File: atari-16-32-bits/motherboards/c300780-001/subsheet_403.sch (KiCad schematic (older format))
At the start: 43 parts, among them Q404 2N3904, Q405 2N3904, U403 MC1377_COLOR_TELEVISION_RGB_T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

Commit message: Resolves #6, #9 : Symbol for L403 and Values for PAL system
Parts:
- DL1: value Delay_Line -> Delay Line 3.58MHz
- L403: value Variable Coil Inductor -> Variable Coil 24uH; symbol Device:L_Core_Iron_Coupled -> variable_coil_shielded:Variable_Coil_Shielded
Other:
- note added: "About L403 and DL1 : I made custom symbols to match the pins written on the schematics.\n\nFor DL1, I once again relied on the schematics of the Falcon030, that is more readable, and seems to have been reused from previous model (I took a chance that they followed \nthe principle 'do not change something that works')\n\nPinout and footprint of 403 seems to be like http://www.gekade.com/downloads/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"
- note added: "Change values for PAL (I took them from the Falcon030 service manual\nafter checking that this part of the schematics is the same as the\nSTe - lucky me)\n\n* C421 : 100pF\n* DL1 : 4.43MHz\n* L403 : 14uH\n* R451 : 22\n* R456 : 1K8 (PAL-I) ; 2K7 (PAL-B)\n* R463 : 1K2\n\nDid you know there was several PAL variant ? \n* PAL-I is for UK/Ireland\n* PAL-B is for Western Europe, Australia and New Zealand"
- note removed: "About L403 and DL1 : I used some built-in look alike symbols, as I could not find for sure an exact reference about those components.\n\n* L403 : \n NTSC => part C100210 - variable coil 24uH \n PAL => part C100214 - variable coil 14uH\n* DL1 :\n NTSC => part C100209 - Delay line 3.58MHz \n PAL => part C100213 - Delay line 4.43MHz\n\nPinout and footprint of 403 seems to be like http://www.gekade.c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"
- note removed: "Change values for PAL : C421, DL1, L403, R451, R456, R483\n(TODO : check values for PAL)"
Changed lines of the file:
@@
 P 2000 6600
 F 0 "DL1" H 2100 6650 50  0000 L CNN
-F 1 "Delay_Line" H 2100 6550 50  0000 L CNN
+F 1 "Delay Line 3.58MHz" H 2100 6550 50  0000 L CNN
 F 2 "" H 2000 6600 50  0001 C CNN
 F 3 "~" H 2000 6600 50  0001 C CNN
@@
 Text Label 5400 8050 1    50   ~ 0
 GND
-$Comp
-L Device:L_Core_Iron_Coupled L403
-U 1 1 60C25168
-P 4900 7650
-F 0 "L403" H 4900 7825 50  0000 C CNN
-F 1 "Variable Coil Inductor" H 4900 7450 50  0000 C CNN
-F 2 "" H 4900 7650 50  0001 C CNN
-F 3 "~" H 4900 7650 50  0001 C CNN
-	1    4900 7650
-	-1   0    0    1
-$EndComp
 Wire Wire Line
 	3400 7150 3900 7150
@@
 Wire Wire Line
 	1400 4600 1400 4850
-Text Notes 700  9750 0    50   ~ 0
-About L403 and DL1 : I used some built-in look alike symbols, as I could not find for sure an exact reference about those components.\n\n* L403 : \n    NTSC => part C100210 - variable coil 24uH \n    PAL  => part C100214 - variable coil 14uH\n* DL1 :\n    NTSC => part C100209 - Delay line 3.58MHz \n    PAL  => part C100213 - Delay line 4.43MHz\n\nPinout and footprint of 403 seems to be like http://www.gekade.com/downloads/to_conscheme.pdf for a 7mm square component. \n\nFootprint of DL1 seems to be like two of coils side by side, with finer pitch.\n\nI am sad that I could not get those component right, I wish you good luck if you need to replace those components or remake a pcb !\n
+Text Notes 700  9900 0    50   ~ 0
+About L403 and DL1 : I made custom symbols to match the pins written on the schematics.\n\nFor DL1, I once again relied on the schematics of the Falcon030, that is more readable, and seems to have been reused from previous model (I took a chance that they followed \nthe principle 'do not change something that works')\n\nPinout and footprint of 403 seems to be like http://www.gekade.com/downloads/to_conscheme.pdf for a 7mm square component with no pin #5. \n\nFootprint of DL1 was made by looking at picture of motherboards without this component and the silk screen of the Atari STe found in a service manual. Because this circuit is \ninstalled on my STE, it would have been too cumbersome for me)\n\nI wish you good luck if you need to replace those components or remake this part of the pcb !\n
 $Comp
 L Connector_Generic_Shielded:Conn_01x03_Shielded MOD
@@
 Text Notes 6950 5250 0    50   ~ 0
 Remove\nfor PAL
-Text Notes 750  8350 0    50   ~ 0
-Change values for PAL : C421, DL1, L403, R451, R456, R483\n(TODO : check values for PAL)
+Text Notes 700  8900 0    50   ~ 0
+Change values for PAL (I took them from the Falcon030 service manual\nafter checking that this part of the schematics is the same as the\nSTe - lucky me)\n\n* C421 : 100pF\n* DL1  : 4.43MHz\n* L403 : 14uH\n* R451 : 22\n* R456 : 1K8 (PAL-I) ; 2K7 (PAL-B)\n* R463 : 1K2\n\nDid you know there was several PAL variant ? \n* PAL-I is for UK/Ireland\n* PAL-B is for Western Europe, Australia and New Zealand
 Text Notes 2150 2750 0    118  ~ 0
 Installed ONLY in systems with modulator
@@
 Text Notes 1150 750  0    118  ~ 0
 Common
+$Comp
+L variable_coil_shielded:Variable_Coil_Shielded L403
+U 1 1 60C25168
+P 4900 7650
+F 0 "L403" H 4900 7825 50  0000 C CNN
+F 1 "Variable Coil 24uH" H 4900 7450 50  0000 C CNN
+F 2 "" H 4900 7650 50  0001 C CNN
+F 3 "~" H 4900 7650 50  0001 C CNN
+	1    4900 7650
+	-1   0    0    1
+$EndComp
 $EndSCHEMATC

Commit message: created symbol for DL1
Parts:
- DL1: symbol Device:Delay_Line -> Delay_Line_Custom_Atari_ST:Delay_Line_Custom_Atari_ST
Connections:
- net GND: now also DL1.9 (COMMUN); no longer DL1.3 (COMMUN)
- net y_in: now also DL1.7; no longer DL1.2
- net at DL1.1: no longer R467.2
- new net: DL1.2, R467.2
- no-connect marks 1 -> 3
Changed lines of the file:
@@
 	5900 6000 5900 6200
 $Comp
-L Device:Delay_Line DL1
+L Delay_Line_Custom_Atari_ST:Delay_Line_Custom_Atari_ST DL1
 U 1 1 60C02EB9
 P 2000 6600
@@
 	-1   0    0    1
 $EndComp
+NoConn ~ 1800 6450
+NoConn ~ 1800 6750
 $EndSCHEMATC

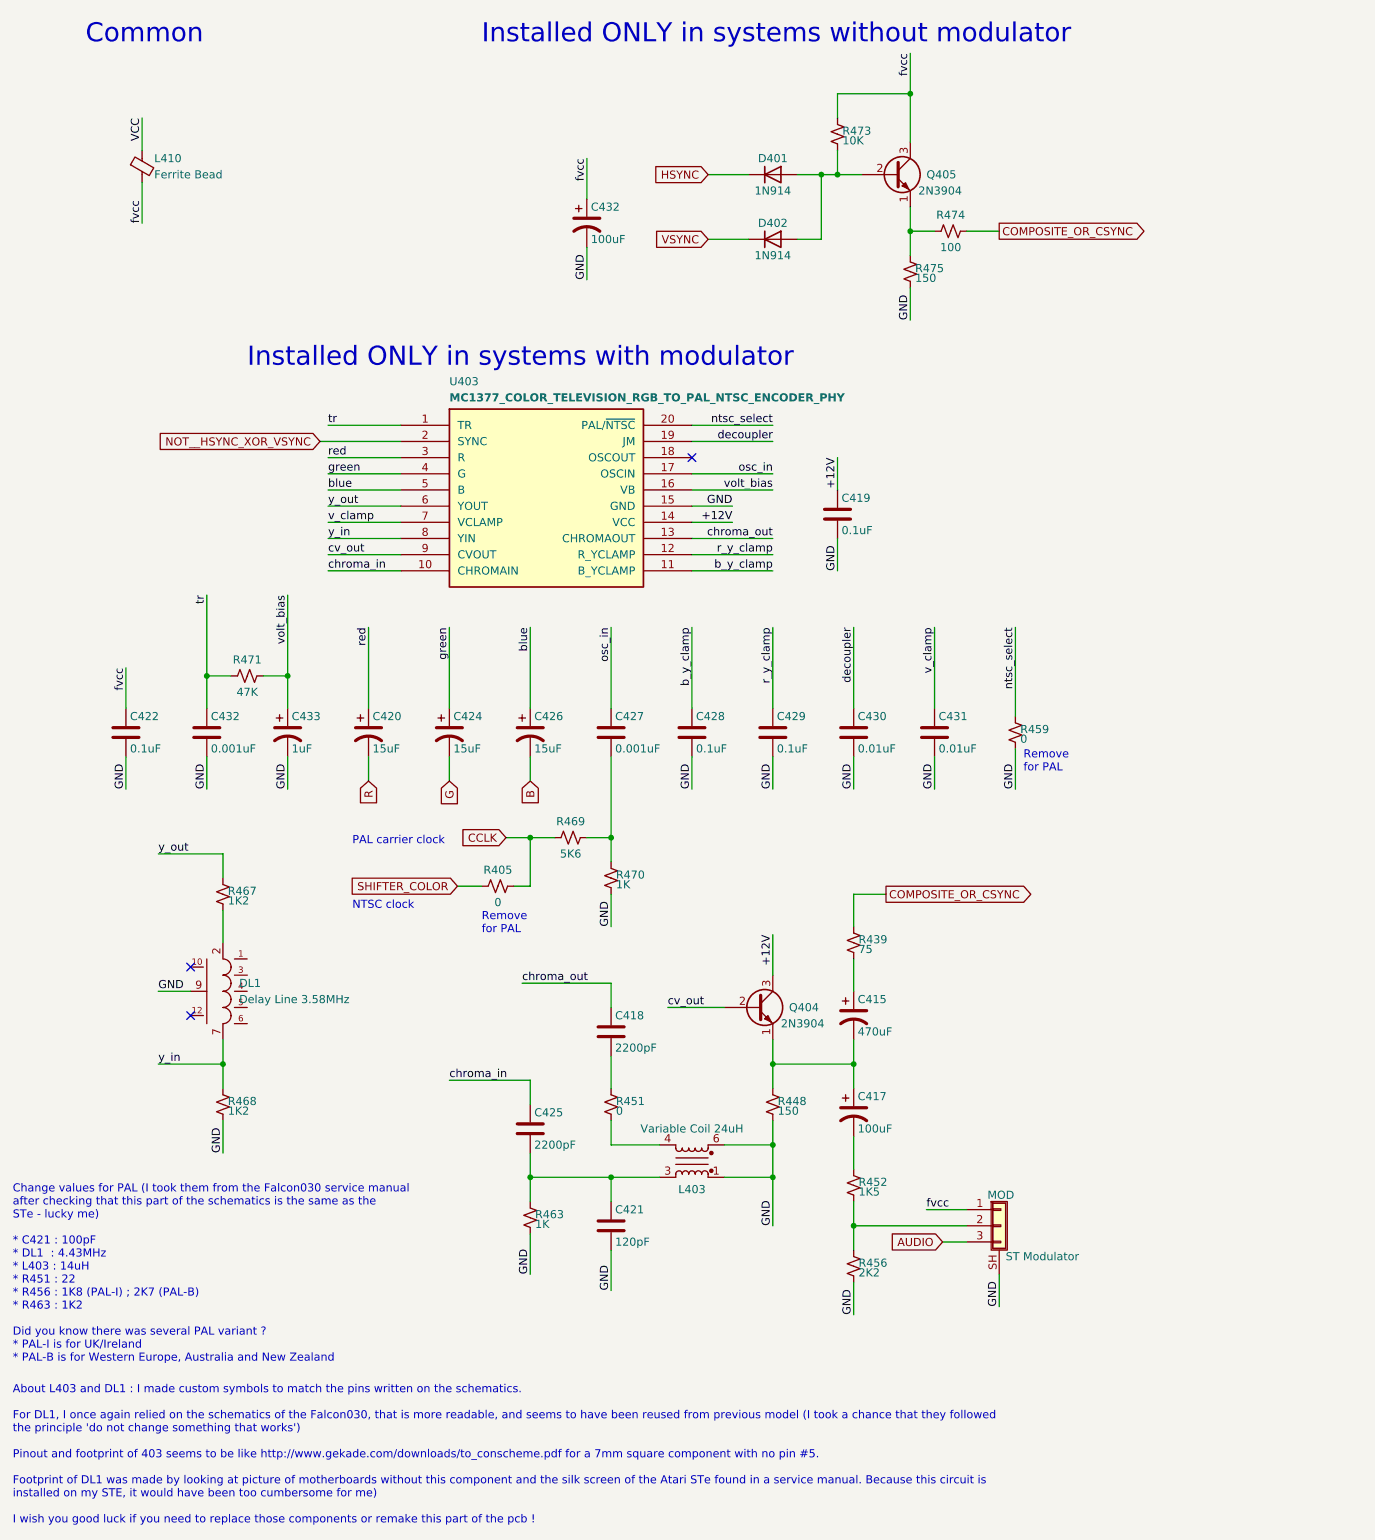
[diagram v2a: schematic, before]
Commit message: updated subsheet 403 : delay line symbol + comments ; subsheet 103 : visual reset circuit
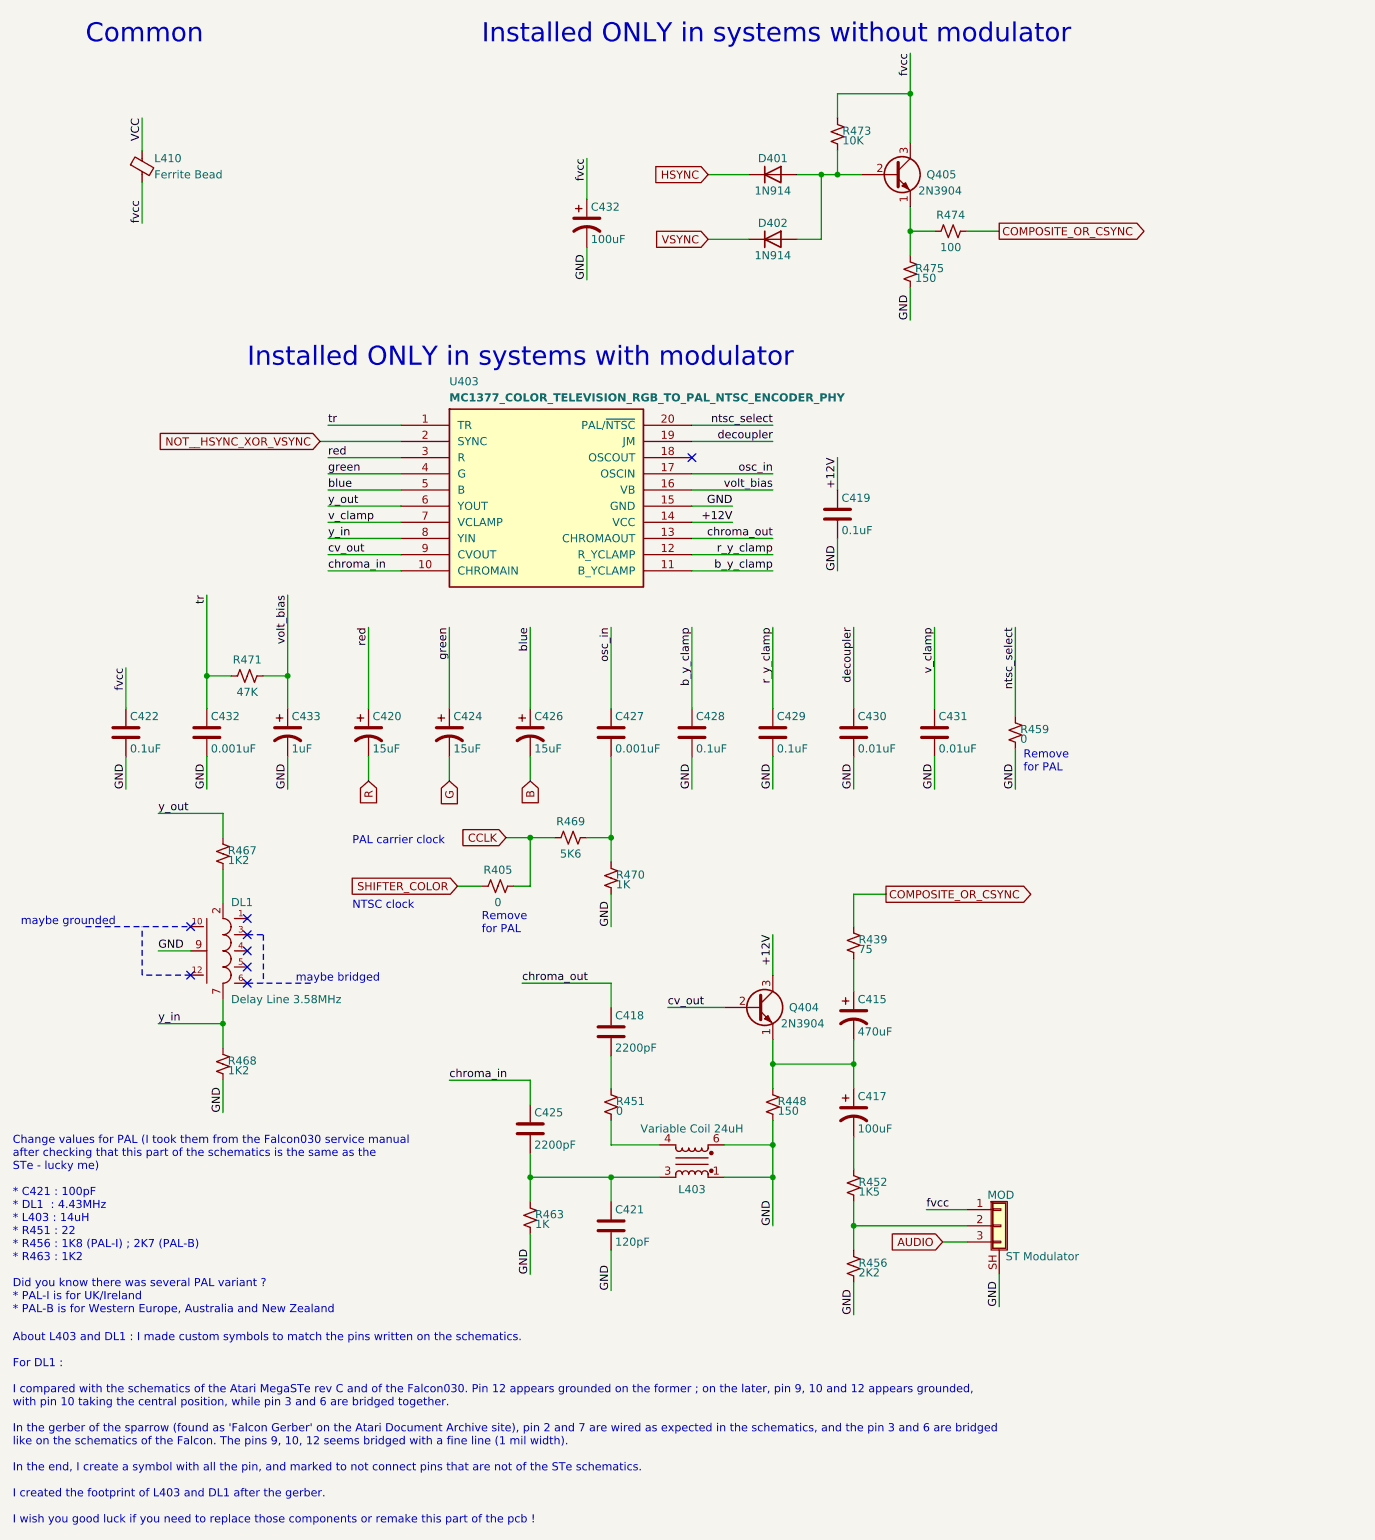
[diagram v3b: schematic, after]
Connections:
- no-connect marks 3 -> 8
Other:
- note added: "About L403 and DL1 : I made custom symbols to match the pins written on the schematics.\n\nFor DL1 : \n\nI compared with the schematics of the Atari MegaSTe rev C and of the Falcon030. Pin 12 appears grounded on the former ; on the later, pin 9, 10 and 12 appears grounded, \nwith pin 10 taking the central position, while pin 3 and 6 are bridged together. \n\nIn the gerber of the sparrow (found as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"
- note added: "maybe bridged"
- note added: "maybe grounded"
- note removed: "About L403 and DL1 : I made custom symbols to match the pins written on the schematics.\n\nFor DL1, I once again relied on the schematics of the Falcon030, that is more readable, and seems to have been reused from previous model (I took a chance that they followed \nthe principle 'do not change something that works')\n\nPinout and footprint of 403 seems to be like http://www.gekade.com/downloads/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"
- moved on the sheet: DL1, R467, R468
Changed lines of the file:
@@
 L Delay_Line_Custom_Atari_ST:Delay_Line_Custom_Atari_ST DL1
 U 1 1 60C02EB9
-P 2000 6600
-F 0 "DL1" H 2100 6650 50  0000 L CNN
-F 1 "Delay Line 3.58MHz" H 2100 6550 50  0000 L CNN
-F 2 "" H 2000 6600 50  0001 C CNN
-F 3 "~" H 2000 6600 50  0001 C CNN
-	1    2000 6600
-	1    0    0    -1
-$EndComp
-Text Label 1600 5750 0    50   ~ 0
+P 2000 6350
+F 0 "DL1" H 2050 6650 50  0000 L CNN
+F 1 "Delay Line 3.58MHz" H 2050 6050 50  0000 L CNN
+F 2 "" H 2000 6350 50  0001 C CNN
+F 3 "~" H 2000 6350 50  0001 C CNN
+	1    2000 6350
+	1    0    0    -1
+$EndComp
+Text Label 1600 5500 0    50   ~ 0
 y_out
 $Comp
 L Device:R_Small_US R?
 U 1 1 60C054F5
-P 2000 6000
+P 2000 5750
 AR Path="/60B3D9E3/60C054F5" Ref="R?"  Part="1"
 AR Path="/60B8B7AD/60C054F5" Ref="R467"  Part="1"
-F 0 "R467" H 2030 6020 50  0000 L CNN
-F 1 "1K2" H 2030 5960 50  0000 L CNN
-F 2 "" H 2000 6000 50  0001 C CNN
-F 3 "~" H 2000 6000 50  0001 C CNN
-	1    2000 6000
-	1    0    0    -1
-$EndComp
-Text Label 1600 7050 0    50   ~ 0
+F 0 "R467" H 2030 5770 50  0000 L CNN
+F 1 "1K2" H 2030 5710 50  0000 L CNN
+F 2 "" H 2000 5750 50  0001 C CNN
+F 3 "~" H 2000 5750 50  0001 C CNN
+	1    2000 5750
+	1    0    0    -1
+$EndComp
+Text Label 1600 6800 0    50   ~ 0
 y_in
 $Comp
 L Device:R_Small_US R?
 U 1 1 60C05DC5
-P 2000 7300
+P 2000 7050
 AR Path="/60B3D9E3/60C05DC5" Ref="R?"  Part="1"
 AR Path="/60B8B7AD/60C05DC5" Ref="R468"  Part="1"
-F 0 "R468" H 2030 7320 50  0000 L CNN
-F 1 "1K2" H 2030 7260 50  0000 L CNN
-F 2 "" H 2000 7300 50  0001 C CNN
-F 3 "~" H 2000 7300 50  0001 C CNN
-	1    2000 7300
-	1    0    0    -1
-$EndComp
-Text Label 2000 7600 1    50   ~ 0
-GND
-Wire Wire Line
-	2000 7400 2000 7600
-Text Label 1600 6600 0    50   ~ 0
-GND
-Wire Wire Line
-	1600 6600 1800 6600
-Wire Wire Line
-	1600 5750 2000 5750
-Wire Wire Line
-	2000 5750 2000 5900
-Wire Wire Line
-	2000 6100 2000 6300
-Wire Wire Line
-	2000 6900 2000 7050
-Wire Wire Line
-	1600 7050 2000 7050
-Connection ~ 2000 7050
-Wire Wire Line
-	2000 7050 2000 7200
+F 0 "R468" H 2030 7070 50  0000 L CNN
+F 1 "1K2" H 2030 7010 50  0000 L CNN
+F 2 "" H 2000 7050 50  0001 C CNN
+F 3 "~" H 2000 7050 50  0001 C CNN
+	1    2000 7050
+	1    0    0    -1
+$EndComp
+Text Label 2000 7350 1    50   ~ 0
+GND
+Wire Wire Line
+	2000 7150 2000 7350
+Text Label 1600 6350 0    50   ~ 0
+GND
+Wire Wire Line
+	1600 6350 1800 6350
+Wire Wire Line
+	1600 5500 2000 5500
+Wire Wire Line
+	2000 5500 2000 5650
+Wire Wire Line
+	2000 5850 2000 6050
+Wire Wire Line
+	2000 6650 2000 6800
+Wire Wire Line
+	1600 6800 2000 6800
+Connection ~ 2000 6800
+Wire Wire Line
+	2000 6800 2000 6950
 $Comp
 L Device:Ferrite_Bead_Small L?
@@
 	1400 4600 1400 4850
 Text Notes 700  9900 0    50   ~ 0
-About L403 and DL1 : I made custom symbols to match the pins written on the schematics.\n\nFor DL1, I once again relied on the schematics of the Falcon030, that is more readable, and seems to have been reused from previous model (I took a chance that they followed \nthe principle 'do not change something that works')\n\nPinout and footprint of 403 seems to be like http://www.gekade.com/downloads/to_conscheme.pdf for a 7mm square component with no pin #5. \n\nFootprint of DL1 was made by looking at picture of motherboards without this component and the silk screen of the Atari STe found in a service manual. Because this circuit is \ninstalled on my STE, it would have been too cumbersome for me)\n\nI wish you good luck if you need to replace those components or remake this part of the pcb !\n
+About L403 and DL1 : I made custom symbols to match the pins written on the schematics.\n\nFor DL1 : \n\nI compared with the schematics of the Atari MegaSTe rev C and of the Falcon030. Pin 12 appears grounded on the former ; on the later, pin 9, 10 and 12 appears grounded, \nwith pin 10 taking the central position, while pin 3 and 6 are bridged together. \n\nIn the gerber of the sparrow (found as 'Falcon Gerber' on the Atari Document Archive site), pin 2 and 7 are wired as expected in the schematics, and the pin 3 and 6 are bridged \nlike on the schematics of the Falcon. The pins 9, 10, 12 seems bridged with a fine line (1 mil width).\n\nIn the end, I create a symbol with all the pin, and marked to not connect pins that are not of the STe schematics.\n\nI created the footprint of L403 and DL1 after the gerber.\n\nI wish you good luck if you need to replace those components or remake this part of the pcb !\n
 $Comp
 L Connector_Generic_Shielded:Conn_01x03_Shielded MOD
@@
 Text Notes 6950 5250 0    50   ~ 0
 Remove\nfor PAL
-Text Notes 700  8900 0    50   ~ 0
+Text Notes 700  8600 0    50   ~ 0
 Change values for PAL (I took them from the Falcon030 service manual\nafter checking that this part of the schematics is the same as the\nSTe - lucky me)\n\n* C421 : 100pF\n* DL1  : 4.43MHz\n* L403 : 14uH\n* R451 : 22\n* R456 : 1K8 (PAL-I) ; 2K7 (PAL-B)\n* R463 : 1K2\n\nDid you know there was several PAL variant ? \n* PAL-I is for UK/Ireland\n* PAL-B is for Western Europe, Australia and New Zealand
 Text Notes 2150 2750 0    118  ~ 0
@@
 	-1   0    0    1
 $EndComp
-NoConn ~ 1800 6450
-NoConn ~ 1800 6750
+NoConn ~ 1800 6200
+NoConn ~ 1800 6500
+NoConn ~ 2150 6150
+NoConn ~ 2150 6250
+NoConn ~ 2150 6350
+NoConn ~ 2150 6450
+NoConn ~ 2150 6550
+Text Notes 750  6200 0    50   ~ 0
+maybe grounded
+Wire Notes Line
+	1800 6500 1500 6500
+Wire Notes Line
+	1500 6500 1500 6200
+Wire Notes Line
+	2150 6250 2250 6250
+Wire Notes Line
+	2250 6250 2250 6550
+Text Notes 2450 6550 0    50   ~ 0
+maybe bridged
+Wire Notes Line
+	1150 6200 1800 6200
+Wire Notes Line
+	2150 6550 2550 6550
 $EndSCHEMATC
